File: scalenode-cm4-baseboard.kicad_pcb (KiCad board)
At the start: 4 copper layers, 135.5 x 40 mm, 147 parts, among them IC1 TPS2378DDA, J1 B2B-XH-A_LF__SN_, J10 LSHM-130-01-L-RH-A-S-K-TR, J3 1-2199230-6, J4 1140084168, J5 0473460001, J6 SS-74800-144, J7 DF40HC(3.0)-100DS-0.4v, J8 DF40HC(3.0)-100DS-0.4v, Q6 BSS138-7-F, U1 TS3USB30EDGSR, U2 AP62301WU-7, U3 TPS2373-3RGW, U4 URB4805YMD-30WR3, U5 TS3USB30EDGSR, U6 FT234XD-R

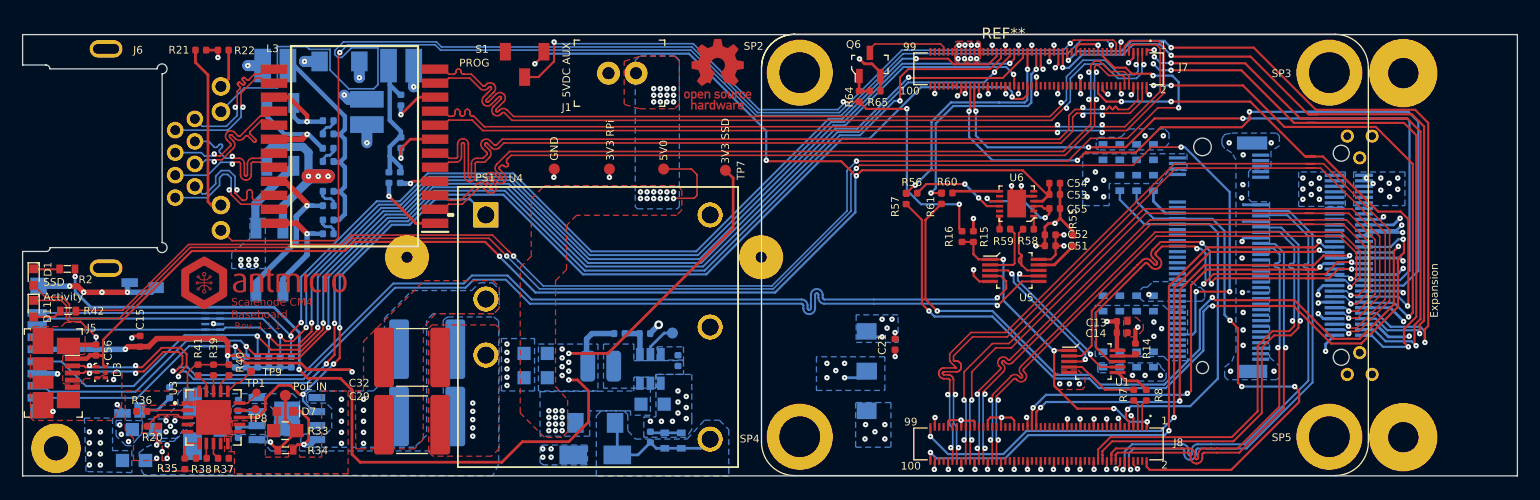
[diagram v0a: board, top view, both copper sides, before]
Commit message: Tune difff pairs and Realocate zones
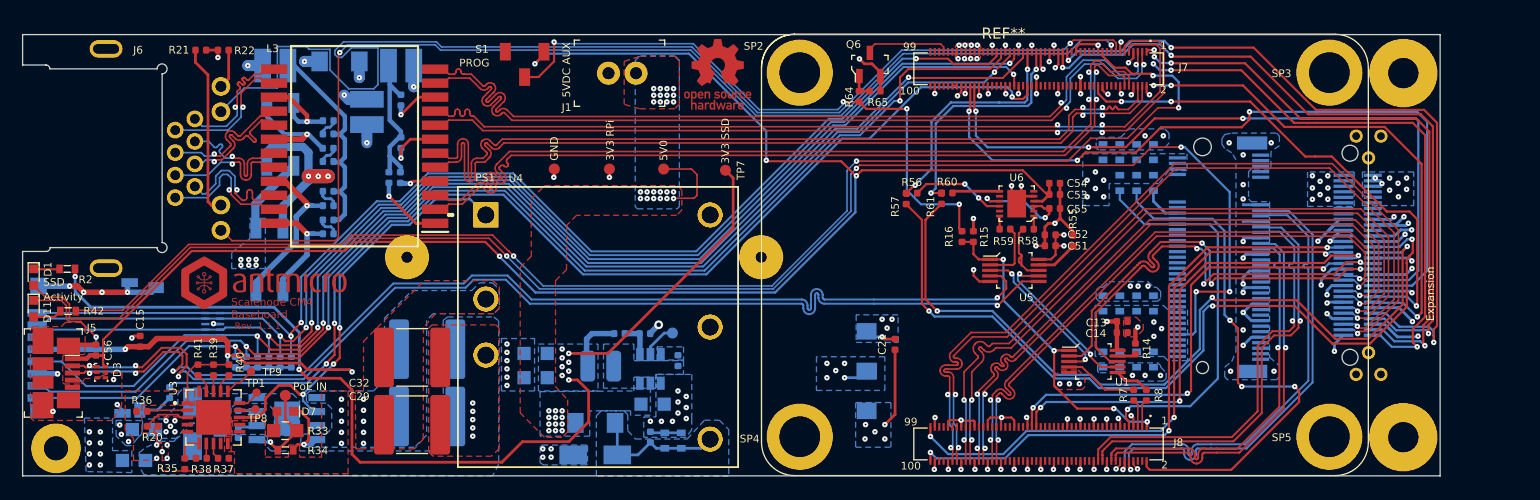
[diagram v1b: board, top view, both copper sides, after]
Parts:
- moved J10 0.80 mm to (195.4, 76.7)
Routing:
- net GND: track 145.3 -> 170.7 mm, vias 125 -> 132
- net 3V3_SSD: track 98.0 -> 104.6 mm, vias 25 -> 24
- net HDMI0_D0_N: track 64.4 -> 65.9 mm, vias 6 -> 3
- net HDMI0_D0_P: track 62.6 -> 64.1 mm
- net HDMI0_D1_N: track 59.9 -> 60.8 mm
- net HDMI0_D1_P: track 57.5 -> 58.5 mm
- net HDMI0_CEC: track 43.0 -> 43.8 mm
- net GPIO7: track 64.5 -> 65.3 mm
- net GPIO18: track 57.3 -> 58.1 mm
- net GPIO24: track 63.0 -> 63.8 mm
- net Adapter_TXD: track 71.9 -> 72.7 mm
- net HDMI0_D2_N: track 53.7 -> 54.4 mm
- net HDMI0_D2_P: track 51.6 -> 52.3 mm
- net 3V3_RPi: track 64.7 -> 65.3 mm, vias 17 -> 16
- net Adapter_RXD: track 74.3 -> 74.9 mm
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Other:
- board size 135.5 x 40 mm -> 128.5 x 40 mm

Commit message: Connect  zones
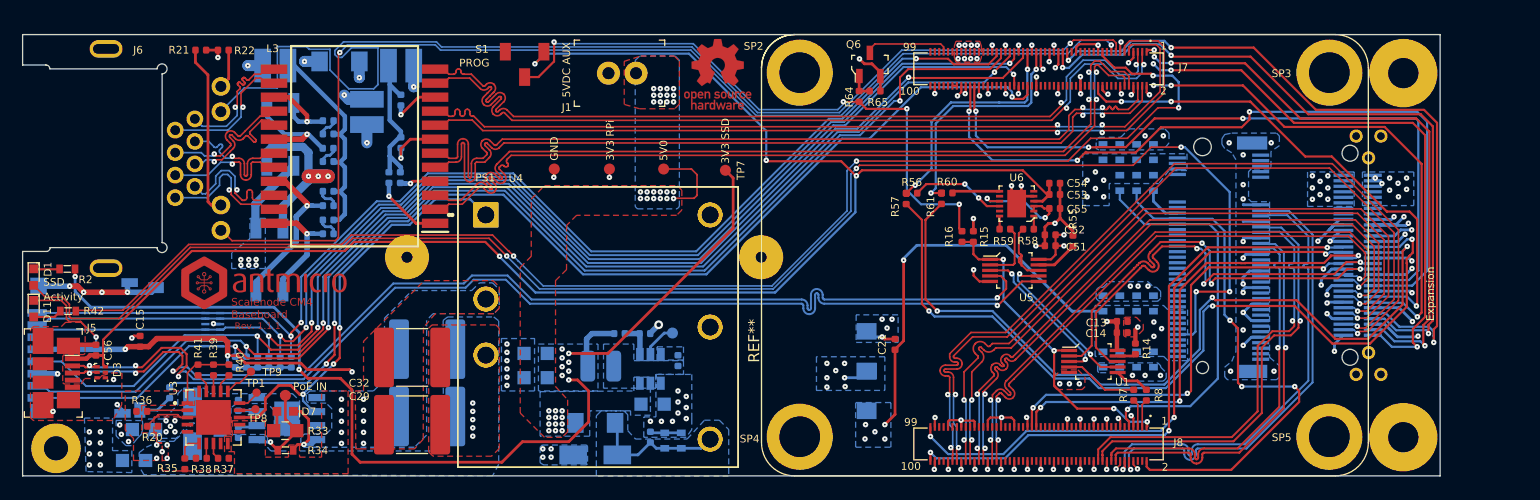
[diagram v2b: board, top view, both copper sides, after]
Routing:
- net 3V3_SSD: track 104.6 -> 134.2 mm, vias 24 -> 25
- net GND: track 170.7 -> 168.7 mm
- net 3V3_OUT: vias 13 -> 15

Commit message: Guide tracks out of vias
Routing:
- net HDMI0_D0_P: track 64.0 -> 65.3 mm
- net HDMI0_D0_N: track 65.9 -> 66.9 mm

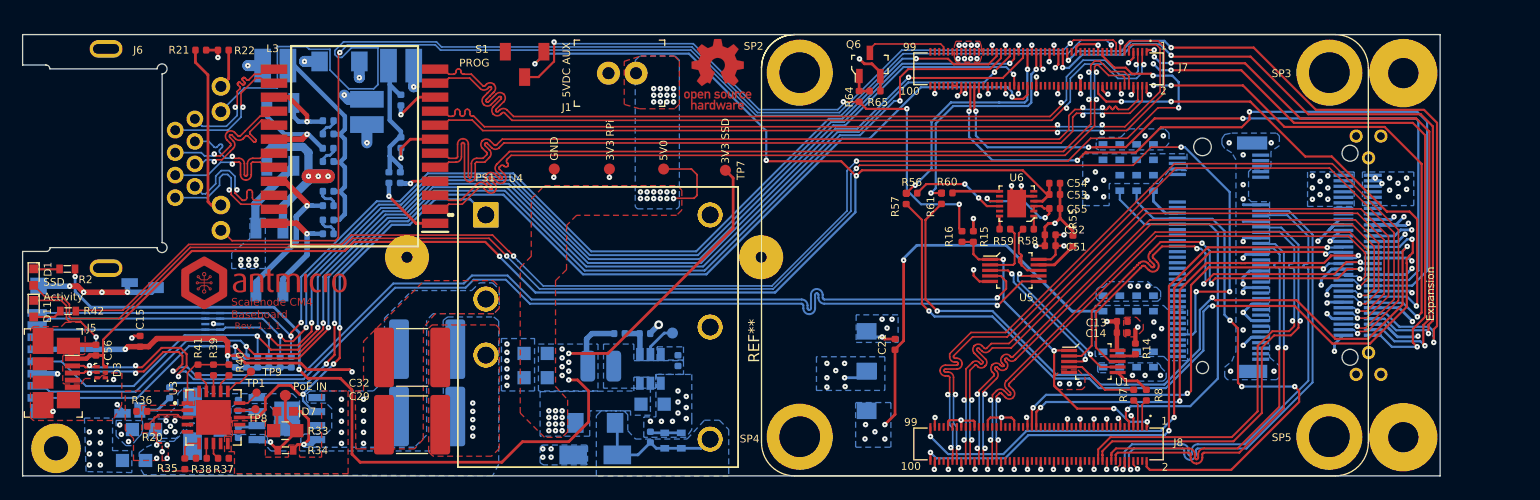
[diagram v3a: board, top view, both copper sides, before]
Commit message: Move U5 to create more space for HDMI routing
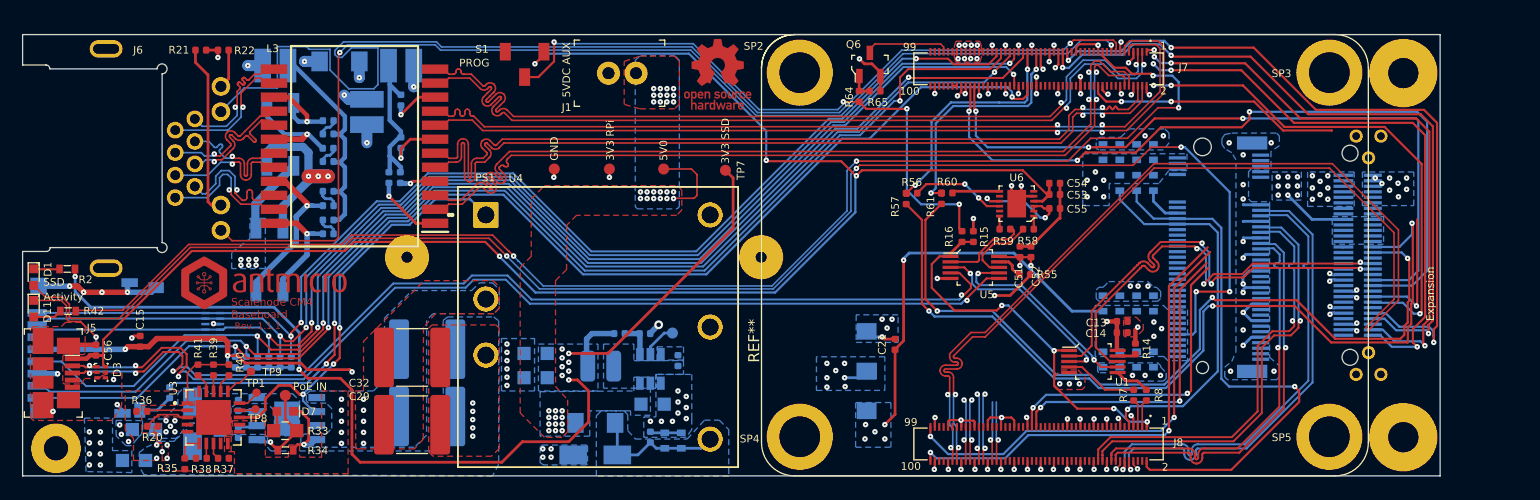
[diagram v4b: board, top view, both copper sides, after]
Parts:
- moved R55 5.32 mm to (165.9, 78.4), turned to 0 degrees
- moved U5 3.60 mm to (161.4, 77.8)
- moved C51 2.79 mm to (165.5, 76.4), turned to 90 degrees
- moved C52 2.33 mm to (166.5, 76.4), turned to 90 degrees
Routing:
- net HDMI0_D0_N: track 66.9 -> 7.88 mm
- net HDMI0_D0_P: track 65.3 -> 7.04 mm
- net HDMI0_D1_N: track 60.4 -> 7.57 mm
- net HDMI0_D1_P: track 58.3 -> 7.57 mm
- net HDMI0_D2_N: track 54.4 -> 6.82 mm, vias 3 -> 2
- net GND: track 168.7 -> 123.2 mm, vias 132 -> 123
- net HDMI0_D2_P: track 52.3 -> 6.82 mm, vias 3 -> 2
- net HDMI0_CEC: track 43.8 -> 28.3 mm, vias 3 -> 2
- net HDMI0_HOTPLUG: track 41.1 -> 28.6 mm, vias 3 -> 2
- net HDMI0_SCL: track 54.2 -> 41.8 mm, vias 3 -> 2
- net HDMI0_SDA: track 53.6 -> 41.4 mm, vias 3 -> 2
- net GPIO26: track 46.5 -> 35.5 mm
- net /Interfaces/CONN_USB_N: track 101.7 -> 95.4 mm
- net /Interfaces/CONN_USB_P: track 99.9 -> 94.3 mm
- net USBOTG_ID: track 30.0 -> 35.5 mm
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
